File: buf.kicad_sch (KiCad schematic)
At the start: 2 parts

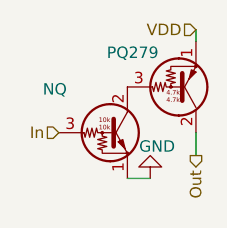
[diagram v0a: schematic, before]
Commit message: Edited Sch, changed buffer from daisy chain to get from root
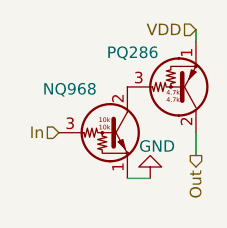
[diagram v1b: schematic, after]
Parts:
- renumbered NQ to NQ968, PQ279 to PQ286
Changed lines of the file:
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@@
 		(on_board yes)
 		(dnp no)
-		(property "Reference" "#PWR028"
+		(property "Reference" "#PWR0613"
 			(at 27.94 30.48 0)
 			(effects
@@
 		(instances
 			(project "RT08-ProgramBoard"
+				(path "/1e4a9b72-5dca-4cd4-9b5c-6a0bbded1998/2016bcd9-6ce1-45f9-8d57-856451ed87a8"
+					(reference "#PWR028")
+					(unit 1)
+				)
+				(path "/1e4a9b72-5dca-4cd4-9b5c-6a0bbded1998/3e0b6698-91dd-4b45-a6a9-afe44cb018de"
+					(reference "#PWR0618")
+					(unit 1)
+				)
+				(path "/1e4a9b72-5dca-4cd4-9b5c-6a0bbded1998/614696c9-19c1-42a8-a8ff-7b461bf6d449"
+					(reference "#PWR0619")
+					(unit 1)
+				)
 				(path "/1e4a9b72-5dca-4cd4-9b5c-6a0bbded1998/8cb9a0e2-ac9e-4f8e-905d-48e2924bf956"
-					(reference "#PWR028")
+					(reference "#PWR0613")
 					(unit 1)
 				)
 				(path "/1e4a9b72-5dca-4cd4-9b5c-6a0bbded1998/936d5558-9fc5-4fc7-a713-5fb79fe91b62"
-					(reference "#PWR030")
+					(reference "#PWR0615")
+					(unit 1)
+				)
+				(path "/1e4a9b72-5dca-4cd4-9b5c-6a0bbded1998/a74b2819-4a0a-42f7-841a-fa52e4c1e7af"
+					(reference "#PWR0616")
 					(unit 1)
 				)
 				(path "/1e4a9b72-5dca-4cd4-9b5c-6a0bbded1998/c3bf8b9b-5e1b-4222-9f14-5fb269051932"
-					(reference "#PWR032")
+					(reference "#PWR0617")
 					(unit 1)
 				)
 				(path "/1e4a9b72-5dca-4cd4-9b5c-6a0bbded1998/f48c2fe5-0d30-48d8-bec9-1dc8a6075678"
-					(reference "#PWR029")
+					(reference "#PWR0614")
 					(unit 1)
 				)
@@
 		(on_board yes)
 		(dnp no)
-		(property "Reference" "PQ279"
+		(property "Reference" "PQ286"
 			(at 23.114 22.86 0)
 			(effects
@@
 		(instances
 			(project "RT08-ProgramBoard"
+				(path "/1e4a9b72-5dca-4cd4-9b5c-6a0bbded1998/2016bcd9-6ce1-45f9-8d57-856451ed87a8"
+					(reference "PQ279")
+					(unit 1)
+				)
+				(path "/1e4a9b72-5dca-4cd4-9b5c-6a0bbded1998/3e0b6698-91dd-4b45-a6a9-afe44cb018de"
+					(reference "PQ284")
+					(unit 1)
+				)
+				(path "/1e4a9b72-5dca-4cd4-9b5c-6a0bbded1998/614696c9-19c1-42a8-a8ff-7b461bf6d449"
+					(reference "PQ285")
+					(unit 1)
+				)
 				(path "/1e4a9b72-5dca-4cd4-9b5c-6a0bbded1998/8cb9a0e2-ac9e-4f8e-905d-48e2924bf956"
-					(reference "PQ279")
+					(reference "PQ286")
 					(unit 1)
 				)
 				(path "/1e4a9b72-5dca-4cd4-9b5c-6a0bbded1998/936d5558-9fc5-4fc7-a713-5fb79fe91b62"
 					(reference "PQ281")
+					(unit 1)
+				)
+				(path "/1e4a9b72-5dca-4cd4-9b5c-6a0bbded1998/a74b2819-4a0a-42f7-841a-fa52e4c1e7af"
+					(reference "PQ282")
 					(unit 1)
 				)
@@
 		(on_board yes)
 		(dnp no)
-		(property "Reference" "NQ"
+		(property "Reference" "NQ968"
 			(at 16.002 26.924 0)
 			(effects
@@
 		(instances
 			(project "RT08-ProgramBoard"
+				(path "/1e4a9b72-5dca-4cd4-9b5c-6a0bbded1998/2016bcd9-6ce1-45f9-8d57-856451ed87a8"
+					(reference "NQ961")
+					(unit 1)
+				)
+				(path "/1e4a9b72-5dca-4cd4-9b5c-6a0bbded1998/3e0b6698-91dd-4b45-a6a9-afe44cb018de"
+					(reference "NQ966")
+					(unit 1)
+				)
+				(path "/1e4a9b72-5dca-4cd4-9b5c-6a0bbded1998/614696c9-19c1-42a8-a8ff-7b461bf6d449"
+					(reference "NQ967")
+					(unit 1)
+				)
+				(path "/1e4a9b72-5dca-4cd4-9b5c-6a0bbded1998/8cb9a0e2-ac9e-4f8e-905d-48e2924bf956"
+					(reference "NQ968")
+					(unit 1)
+				)
 				(path "/1e4a9b72-5dca-4cd4-9b5c-6a0bbded1998/936d5558-9fc5-4fc7-a713-5fb79fe91b62"
-					(reference "NQ961")
+					(reference "NQ963")
+					(unit 1)
+				)
+				(path "/1e4a9b72-5dca-4cd4-9b5c-6a0bbded1998/a74b2819-4a0a-42f7-841a-fa52e4c1e7af"
+					(reference "NQ964")
 					(unit 1)
 				)
 				(path "/1e4a9b72-5dca-4cd4-9b5c-6a0bbded1998/c3bf8b9b-5e1b-4222-9f14-5fb269051932"
-					(reference "NQ964")
-					(unit 1)
-				)
+					(reference "NQ965")
+					(unit 1)
+				)

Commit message: Editing PCB, one line almost-done?
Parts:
- renumbered NQ968 to NQ961, PQ286 to PQ279
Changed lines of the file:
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@@
 		(on_board yes)
 		(dnp no)
-		(property "Reference" "#PWR0613"
+		(property "Reference" "#PWR?"
 			(at 27.94 30.48 0)
 			(effects
@@
 			(project "RT08-ProgramBoard"
 				(path "/1e4a9b72-5dca-4cd4-9b5c-6a0bbded1998/2016bcd9-6ce1-45f9-8d57-856451ed87a8"
-					(reference "#PWR028")
+					(reference "#PWR?")
 					(unit 1)
 				)
 				(path "/1e4a9b72-5dca-4cd4-9b5c-6a0bbded1998/3e0b6698-91dd-4b45-a6a9-afe44cb018de"
-					(reference "#PWR0618")
+					(reference "#PWR?")
 					(unit 1)
 				)
 				(path "/1e4a9b72-5dca-4cd4-9b5c-6a0bbded1998/614696c9-19c1-42a8-a8ff-7b461bf6d449"
-					(reference "#PWR0619")
+					(reference "#PWR?")
 					(unit 1)
 				)
 				(path "/1e4a9b72-5dca-4cd4-9b5c-6a0bbded1998/8cb9a0e2-ac9e-4f8e-905d-48e2924bf956"
-					(reference "#PWR0613")
+					(reference "#PWR?")
 					(unit 1)
 				)
 				(path "/1e4a9b72-5dca-4cd4-9b5c-6a0bbded1998/936d5558-9fc5-4fc7-a713-5fb79fe91b62"
-					(reference "#PWR0615")
+					(reference "#PWR?")
 					(unit 1)
 				)
 				(path "/1e4a9b72-5dca-4cd4-9b5c-6a0bbded1998/a74b2819-4a0a-42f7-841a-fa52e4c1e7af"
-					(reference "#PWR0616")
+					(reference "#PWR?")
 					(unit 1)
 				)
 				(path "/1e4a9b72-5dca-4cd4-9b5c-6a0bbded1998/c3bf8b9b-5e1b-4222-9f14-5fb269051932"
-					(reference "#PWR0617")
+					(reference "#PWR?")
 					(unit 1)
 				)
 				(path "/1e4a9b72-5dca-4cd4-9b5c-6a0bbded1998/f48c2fe5-0d30-48d8-bec9-1dc8a6075678"
-					(reference "#PWR0614")
+					(reference "#PWR?")
 					(unit 1)
 				)
@@
 		(on_board yes)
 		(dnp no)
-		(property "Reference" "PQ286"
+		(property "Reference" "PQ279"
 			(at 23.114 22.86 0)
 			(effects
@@
 			(project "RT08-ProgramBoard"
 				(path "/1e4a9b72-5dca-4cd4-9b5c-6a0bbded1998/2016bcd9-6ce1-45f9-8d57-856451ed87a8"
-					(reference "PQ279")
+					(reference "PQ286")
 					(unit 1)
 				)
@@
 				)
 				(path "/1e4a9b72-5dca-4cd4-9b5c-6a0bbded1998/8cb9a0e2-ac9e-4f8e-905d-48e2924bf956"
-					(reference "PQ286")
+					(reference "PQ279")
 					(unit 1)
 				)
@@
 		(on_board yes)
 		(dnp no)
-		(property "Reference" "NQ968"
+		(property "Reference" "NQ961"
 			(at 16.002 26.924 0)
 			(effects
@@
 			(project "RT08-ProgramBoard"
 				(path "/1e4a9b72-5dca-4cd4-9b5c-6a0bbded1998/2016bcd9-6ce1-45f9-8d57-856451ed87a8"
-					(reference "NQ961")
+					(reference "NQ968")
 					(unit 1)
 				)
@@
 				)
 				(path "/1e4a9b72-5dca-4cd4-9b5c-6a0bbded1998/8cb9a0e2-ac9e-4f8e-905d-48e2924bf956"
-					(reference "NQ968")
-					(unit 1)
-				)
+					(reference "NQ961")
+					(unit 1)
+				)
